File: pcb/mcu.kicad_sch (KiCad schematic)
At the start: 24 parts, among them J1 LCD, SW1 RESET, SW2 BOOT, U1 ESP32-S3-WROOM-1-N8R2

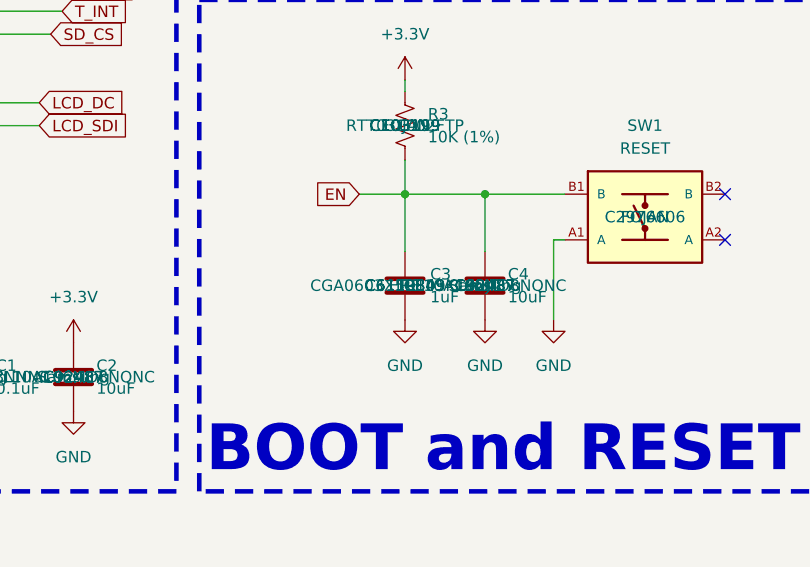
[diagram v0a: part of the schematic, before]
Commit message: Added buzzer
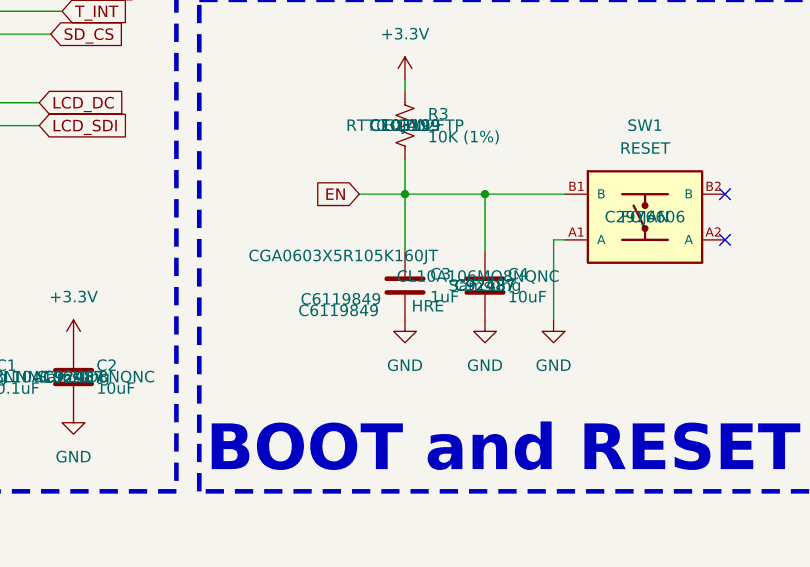
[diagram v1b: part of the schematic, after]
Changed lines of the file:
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@@
 		)
 		(property "MPN" "CL10A106MO8NQNC"
-			(at 168.91 104.14 0)
+			(at 168.148 103.124 0)
 			(effects
 				(font
@@
 		)
 		(property "LCSC" "C6119849"
-			(at 160.02 104.14 0)
+			(at 152.654 106.934 0)
 			(effects
 				(font
@@
 		)
 		(property "LCSC_PN" "C6119849"
-			(at 160.02 104.14 0)
+			(at 152.908 105.664 0)
 			(effects
 				(font
@@
 		)
 		(property "MN" "HRE"
-			(at 160.02 104.14 0)
+			(at 162.56 106.426 0)
 			(effects
 				(font
@@
 		)
 		(property "MPN" "CGA0603X5R105K160JT"
-			(at 160.02 104.14 0)
-			(effects
-				(font
+			(at 153.162 100.838 0)
+			(effects
+				(font

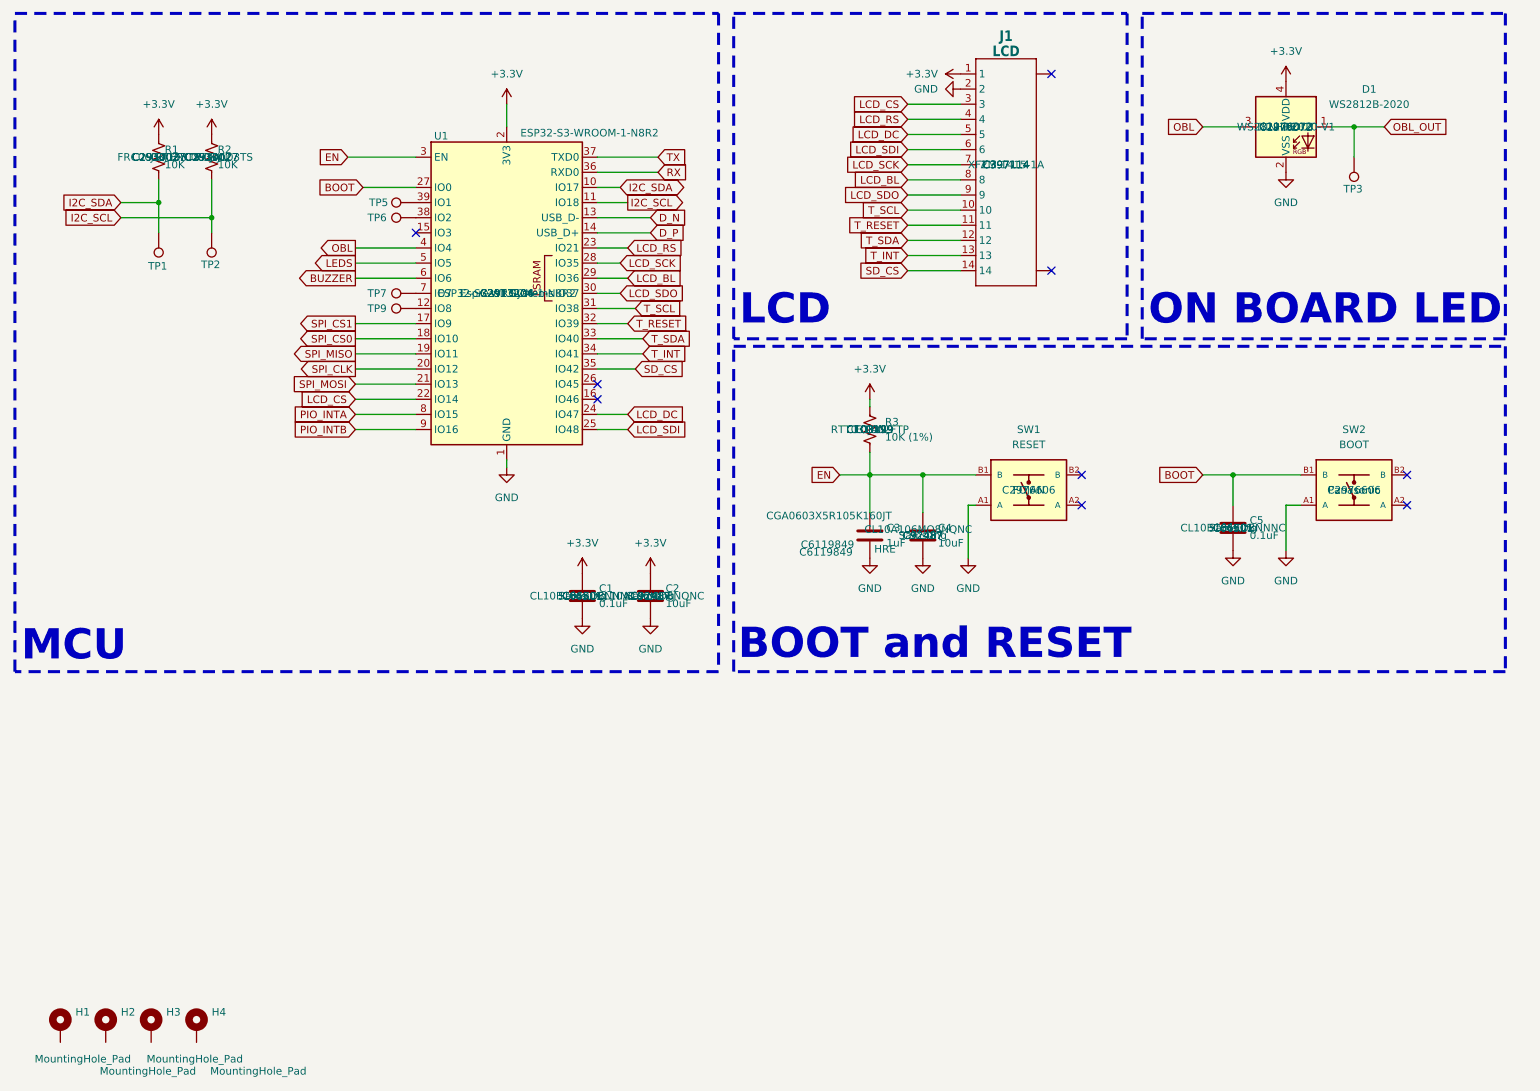
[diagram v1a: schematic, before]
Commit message: Changed SPI to 8 pin connector
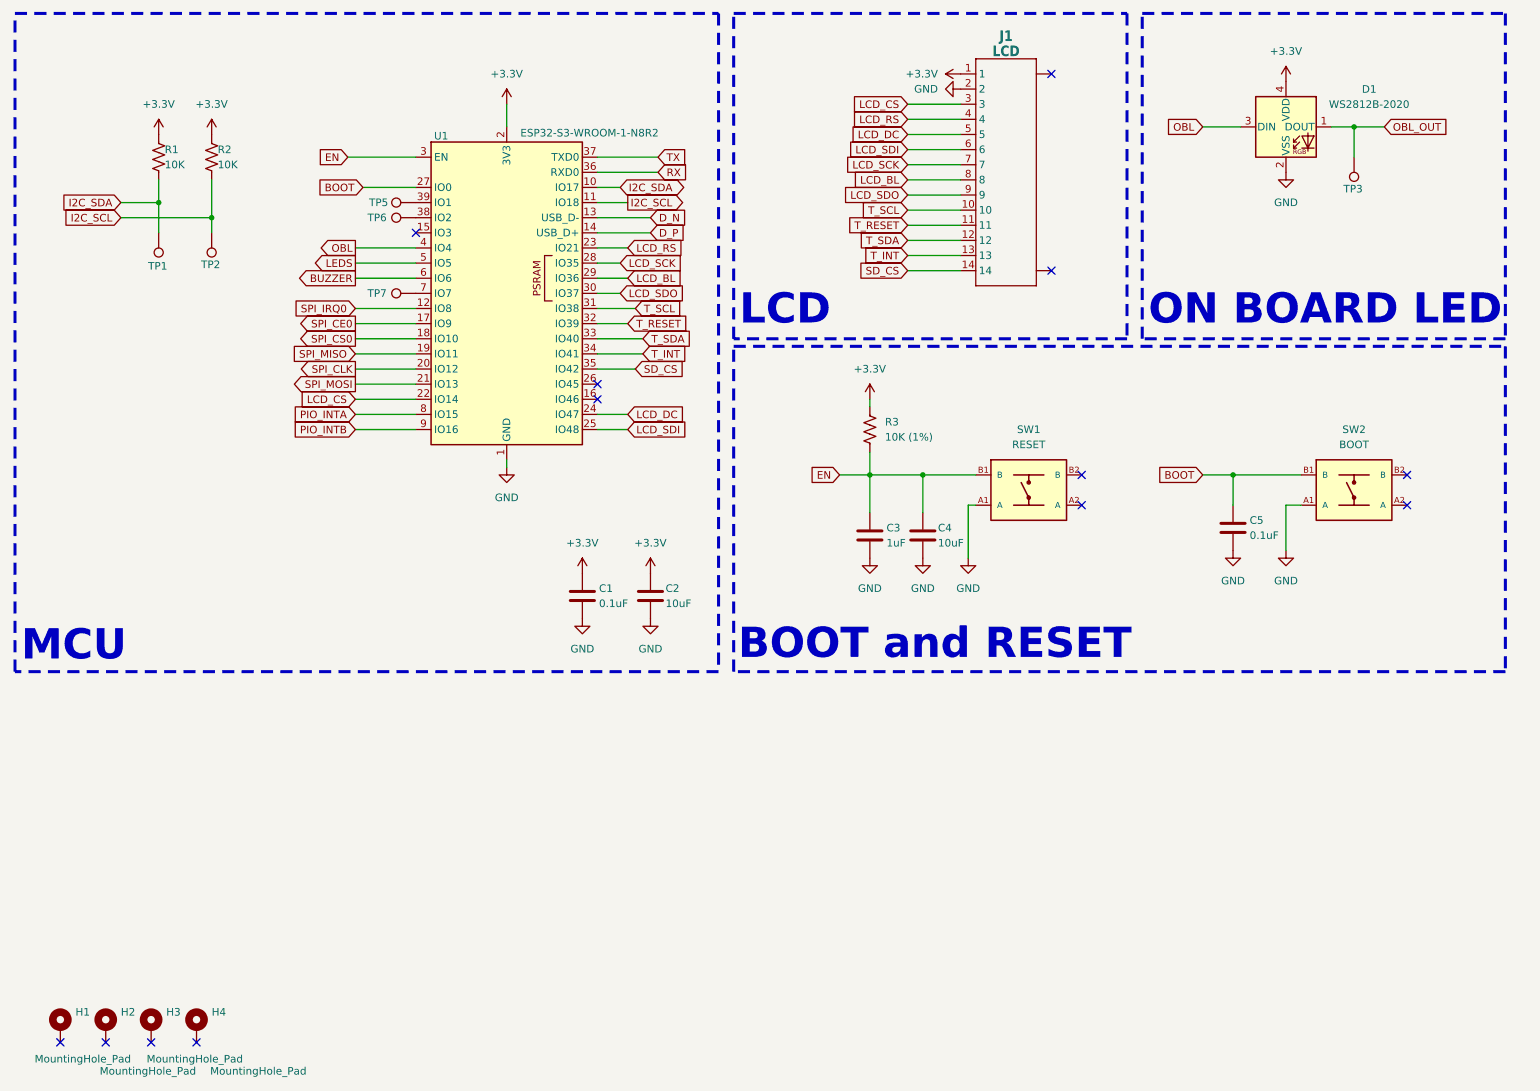
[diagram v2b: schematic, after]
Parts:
- removed TP9: IO8, TestPoint:TestPoint_Pad_D1.0mm, symbol Connector:TestPoint
- TP1, TP2, TP3, TP5, TP6, TP7: now in the parts list
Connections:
- net SPI_IRQ0: now reaches U1.12 (IO8)
- net SPI_CS1 renamed SPI_CE0
- no-connect marks 9 -> 13

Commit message: added open hw; changed test points; added pulls on buttons
change buttons to be 2 connectors with pull ups.
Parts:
- TP1, TP2, TP3, TP7: footprint TestPoint:TestPoint_Pad_D1.0mm -> CRGM Mechanical:TestPoint_Pad_D1.0mm
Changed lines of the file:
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@@
 			)
 		)
-		(property "Footprint" "TestPoint:TestPoint_Pad_D1.0mm"
+		(property "Footprint" "CRGM Mechanical:TestPoint_Pad_D1.0mm"
 			(at 236.22 40.64 0)
 			(effects
@@
 			)
 		)
-		(property "Footprint" "TestPoint:TestPoint_Pad_D1.0mm"
+		(property "Footprint" "CRGM Mechanical:TestPoint_Pad_D1.0mm"
 			(at 35.56 53.34 0)
 			(effects
@@
 			)
 		)
-		(property "Footprint" "TestPoint:TestPoint_Pad_D1.0mm"
+		(property "Footprint" "CRGM Mechanical:TestPoint_Pad_D1.0mm"
 			(at 83.82 58.42 0)
 			(effects
@@
 			)
 		)
-		(property "Footprint" "TestPoint:TestPoint_Pad_D1.0mm"
+		(property "Footprint" "CRGM Mechanical:TestPoint_Pad_D1.0mm"
 			(at 44.45 53.34 0)
 			(effects

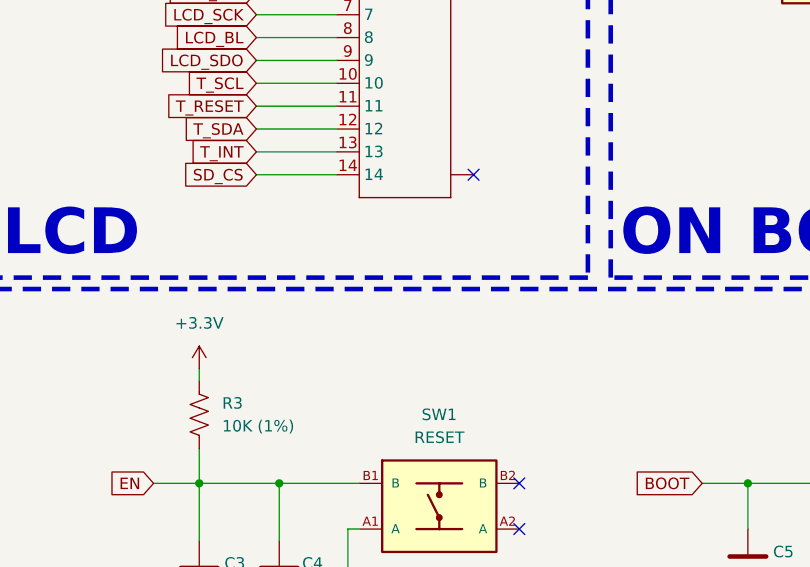
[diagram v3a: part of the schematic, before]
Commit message: Change panel to be 1x1
Changed connectors be vertical rather than horizontal.
Updated TVS diodes to DFN1006 rather than SMF
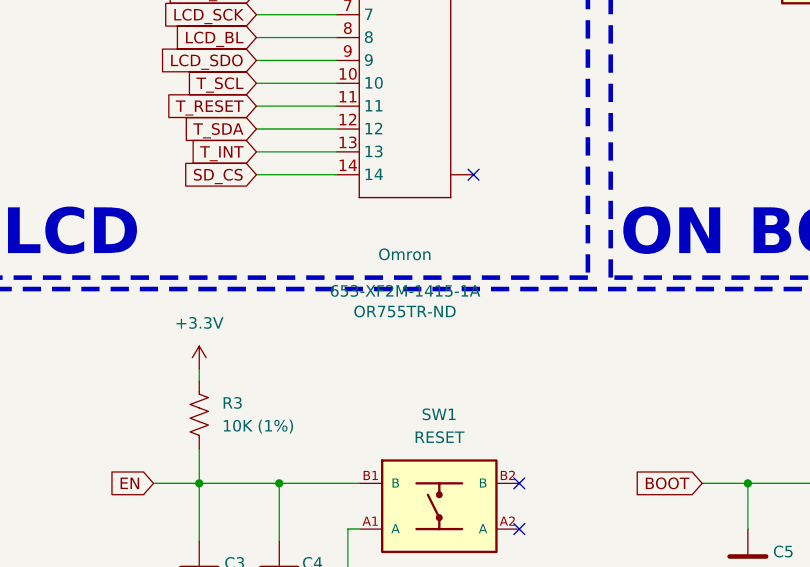
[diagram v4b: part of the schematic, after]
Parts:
- J1: Digikey (none) -> OR755TR-ND; MN (none) -> Omron; Mouser (none) -> 653-XF2M-1415-1A
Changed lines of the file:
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@@
+			)
+		)
+		(property "MN" "Omron"
+			(at 182.88 68.58 0)
+			(effects
+				(font
+					(size 1.27 1.27)
+				)
+			)
+		)
+		(property "Mouser" "653-XF2M-1415-1A"
+			(at 182.88 72.644 0)
+			(effects
+				(font
+					(size 1.27 1.27)
+				)
+			)
+		)
+		(property "Digikey" "OR755TR-ND"
+			(at 182.88 74.93 0)
+			(effects
+				(font
+					(size 1.27 1.27)
+				)
 			)
 		)

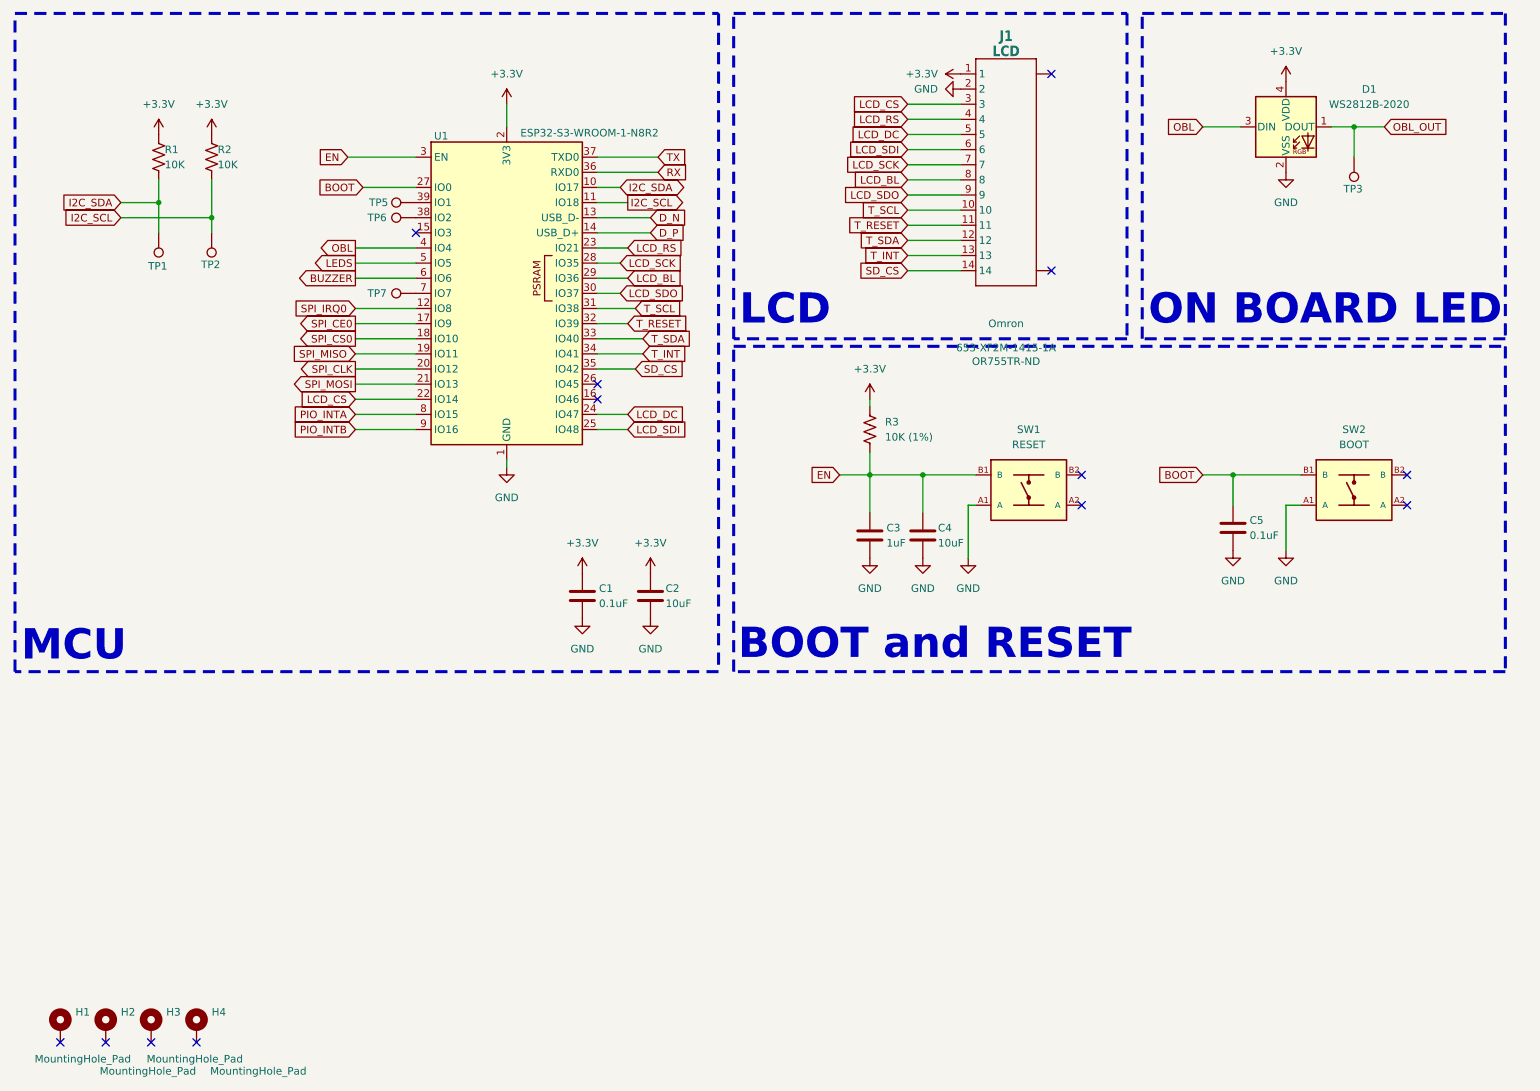
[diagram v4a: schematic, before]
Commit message: Major overhaul of IO
Added GPIO module
Added SPI interface
Added serial interface
Added power selection
Added power LEDs
Changed v3.3 LDO
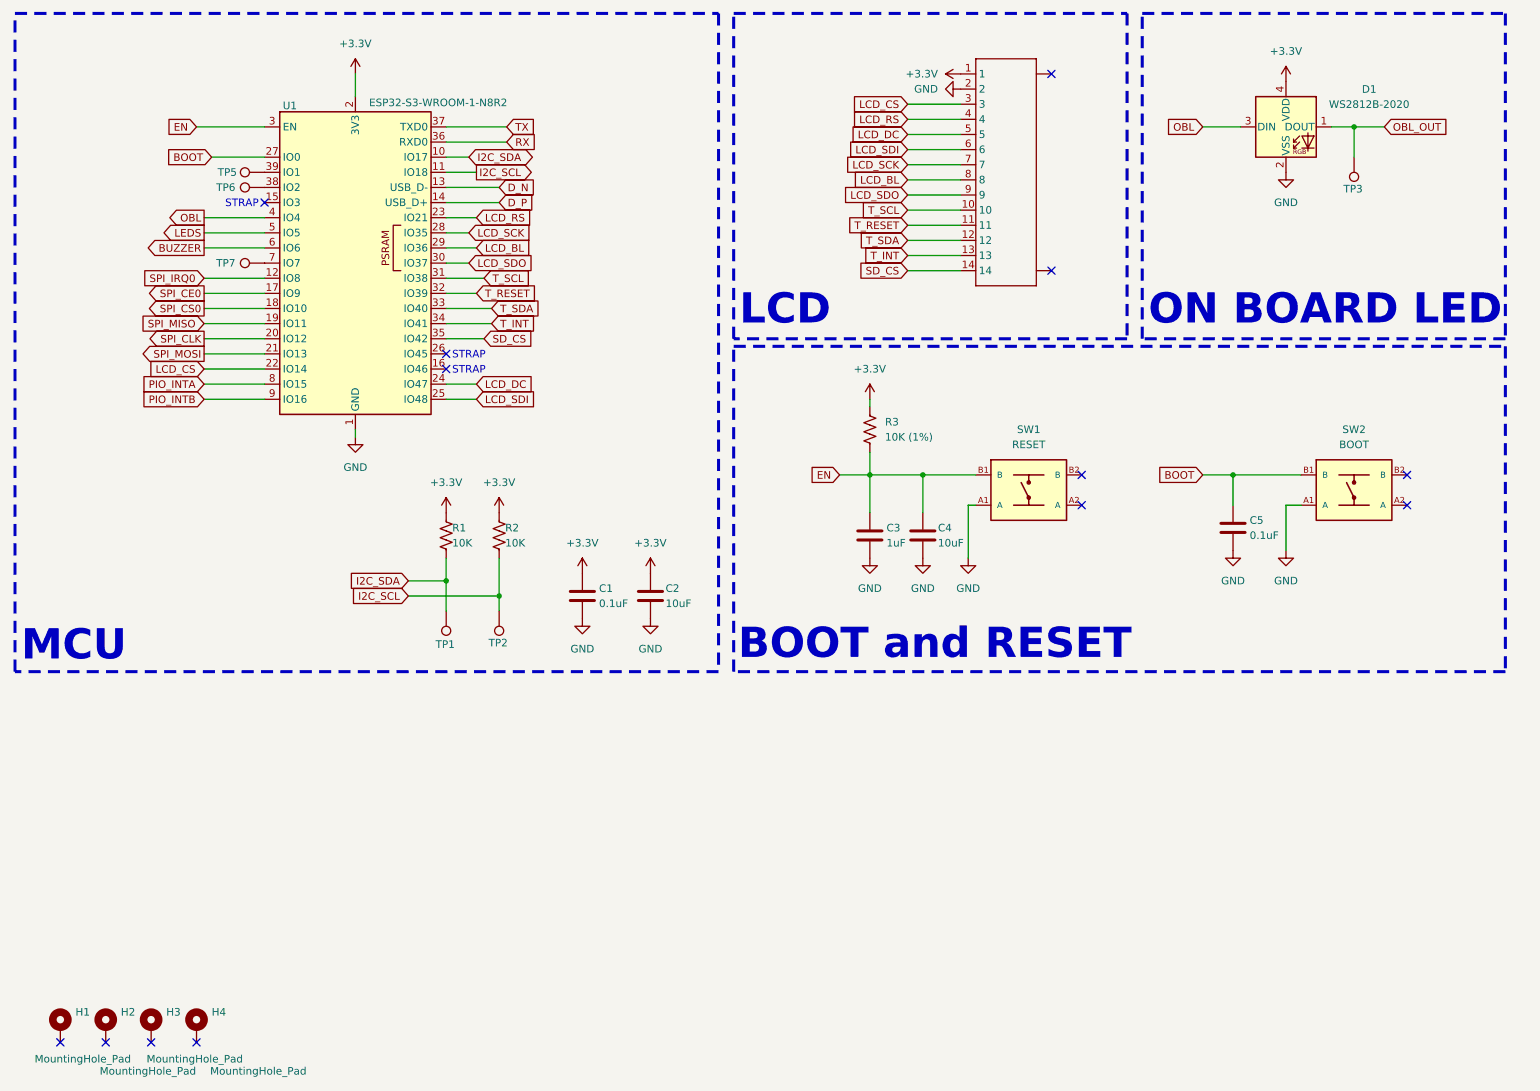
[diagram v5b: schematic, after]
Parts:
- C1: LCSC_PN C66501 -> (none)
- TP5, TP6: footprint TestPoint:TestPoint_Pad_D1.0mm -> CRGM Mechanical:TestPoint_Pad_D1.0mm
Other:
- note added: "STRAP"
- moved on the sheet: R1, R2, TP1, TP2, TP5, TP6, TP7, U1

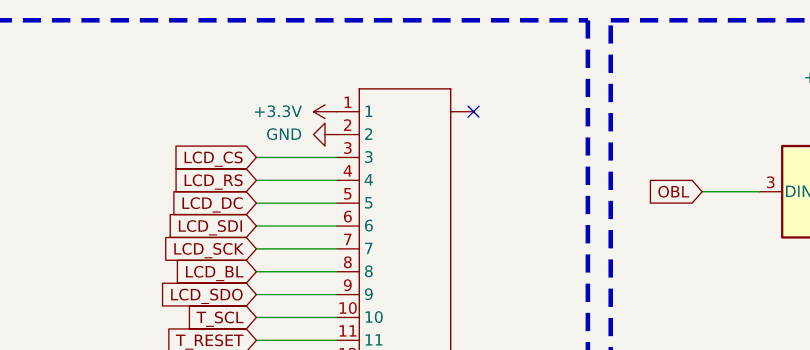
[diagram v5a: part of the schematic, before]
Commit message: Fixed MPN mismatches and other fields
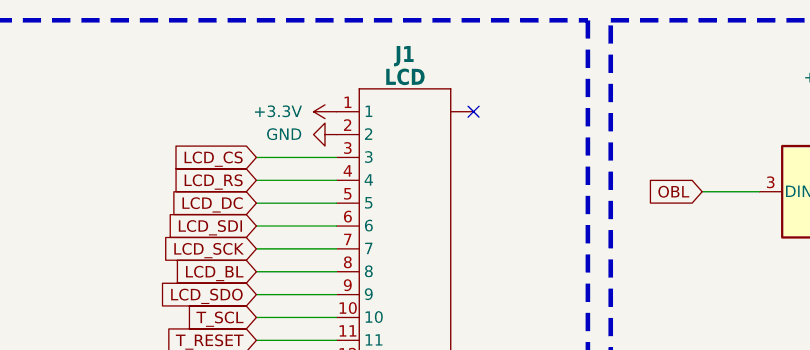
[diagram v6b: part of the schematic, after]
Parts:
- D1: MF World Semi -> HRE
- R1: MN JST -> FOJAN
- SW1: MN FOJAN -> Panasonic
